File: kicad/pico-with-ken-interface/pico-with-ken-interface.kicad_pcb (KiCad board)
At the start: 4 copper layers, 81.3 x 81.3 mm, 10 parts, among them SW2 TSC015A03526A, U1 Pico, U3 XDZ254-2-15-W-2.5-G1, U5 PM254-2-15-W-8.5

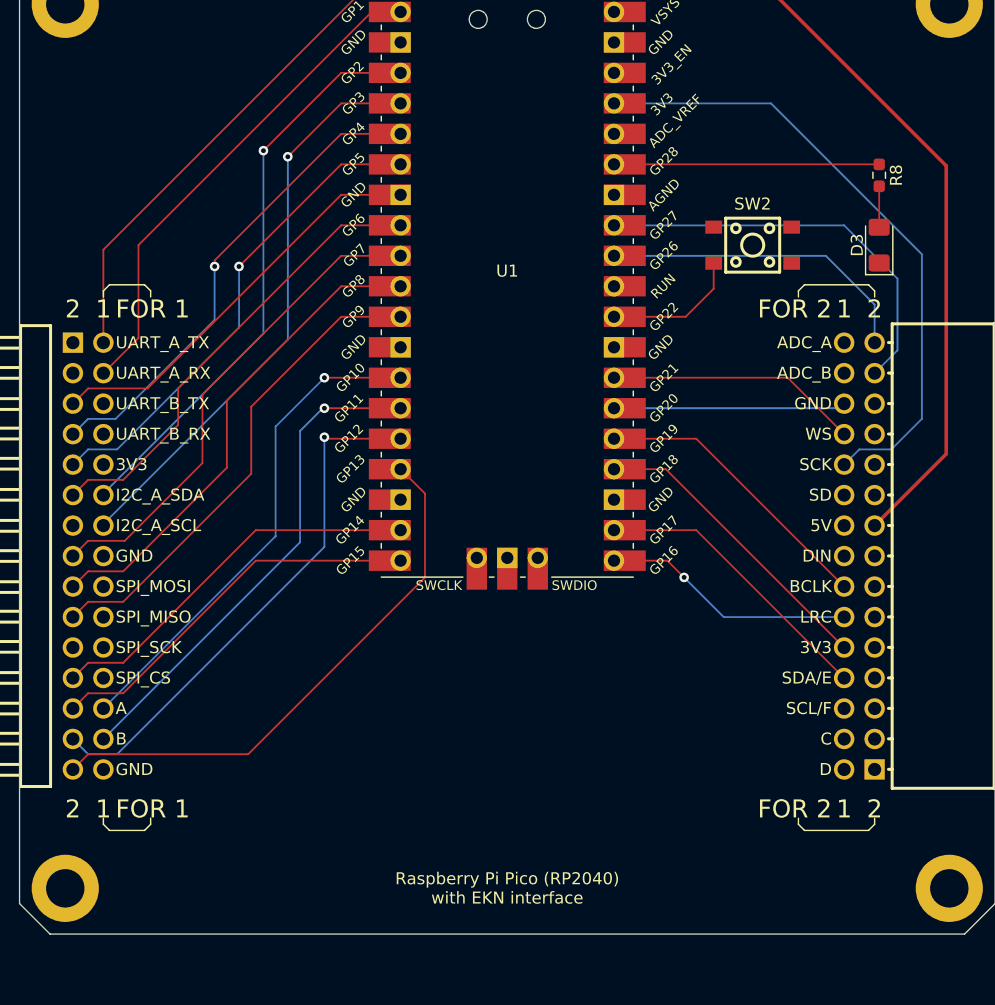
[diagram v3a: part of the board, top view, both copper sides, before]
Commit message: finalize pin assignment for pico board
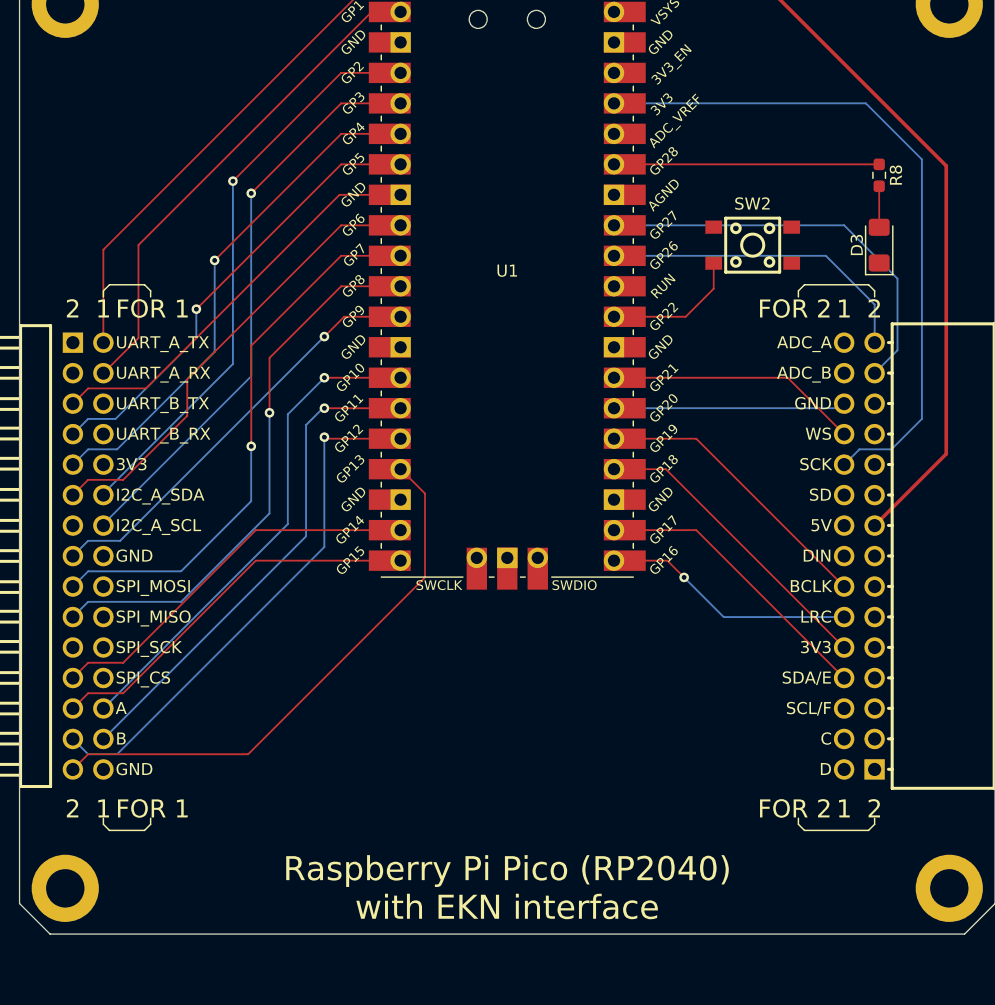
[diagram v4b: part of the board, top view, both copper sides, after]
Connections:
- U3 pad 15: /GPIO7 -> /GPIO9
- U3 pad 17: /GPIO8 -> /GPIO7
- U3 pad 19: /GPIO9 -> /GPIO8
- U3 pad 7: /GPIO4 -> /GPIO5
- U3 pad 9: /GPIO5 -> /GPIO4
- U5 pad 11: /GPIO9 -> /GPIO8
- U5 pad 13: /GPIO8 -> /GPIO7
- U5 pad 15: /GPIO7 -> /GPIO9
- U5 pad 21: /GPIO5 -> /GPIO4
- U5 pad 23: /GPIO4 -> /GPIO5
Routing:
- net +3V3: track 167.8 -> 172.5 mm
- net /GPIO8: track 117.6 -> 122.2 mm, vias 0 -> 1
- net /GPIO7: track 118.5 -> 123.0 mm, vias 0 -> 1
- net /GPIO9: track 116.8 -> 113.1 mm, vias 0 -> 1
- net /GPIO5: track 120.7 -> 118.9 mm
- net /GPIO4: track 121.5 -> 123.2 mm
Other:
- board text added: "version:1.0 date: 20260204"
- board text removed: "version:1.0 date: 20260202"

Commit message: trace adjust
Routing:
- net +5V: track 144.9 -> 145.9 mm

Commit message: ready to send pico board to manufacturing
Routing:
- net /GPIO8: track 122.2 -> 119.2 mm
- net /GPIO7: track 123.0 -> 120.0 mm
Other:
- board text added: "version:1.0 date: 20260211"
- board text removed: "version:1.0 date: 20260204"

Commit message: fix labels, update manufacture files
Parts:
- added kibuzzard-69ABCB94: G***, kibuzzard-69ABCB94, F.Cu at (119.5, 51.4)
- added kibuzzard-69ABCBB2: G***, kibuzzard-69ABCBB2, F.Cu at (130.0, 51.4)
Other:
- board text added: "Raspberry Pi Pico (RP2040) with EKN Interface"
- board text removed: "Raspberry Pi Pico (RP2040) with EKN interface"

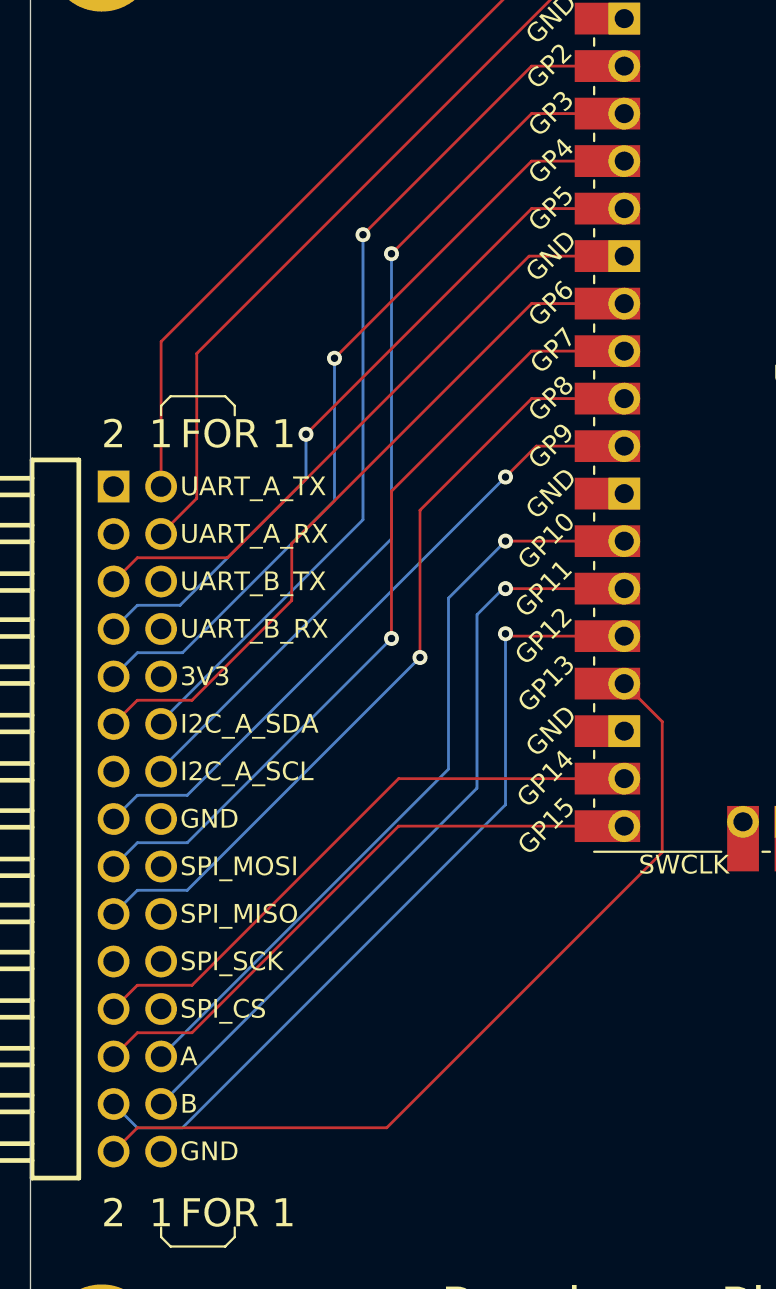
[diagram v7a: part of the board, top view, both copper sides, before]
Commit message: use 4,5 for default I2C pins
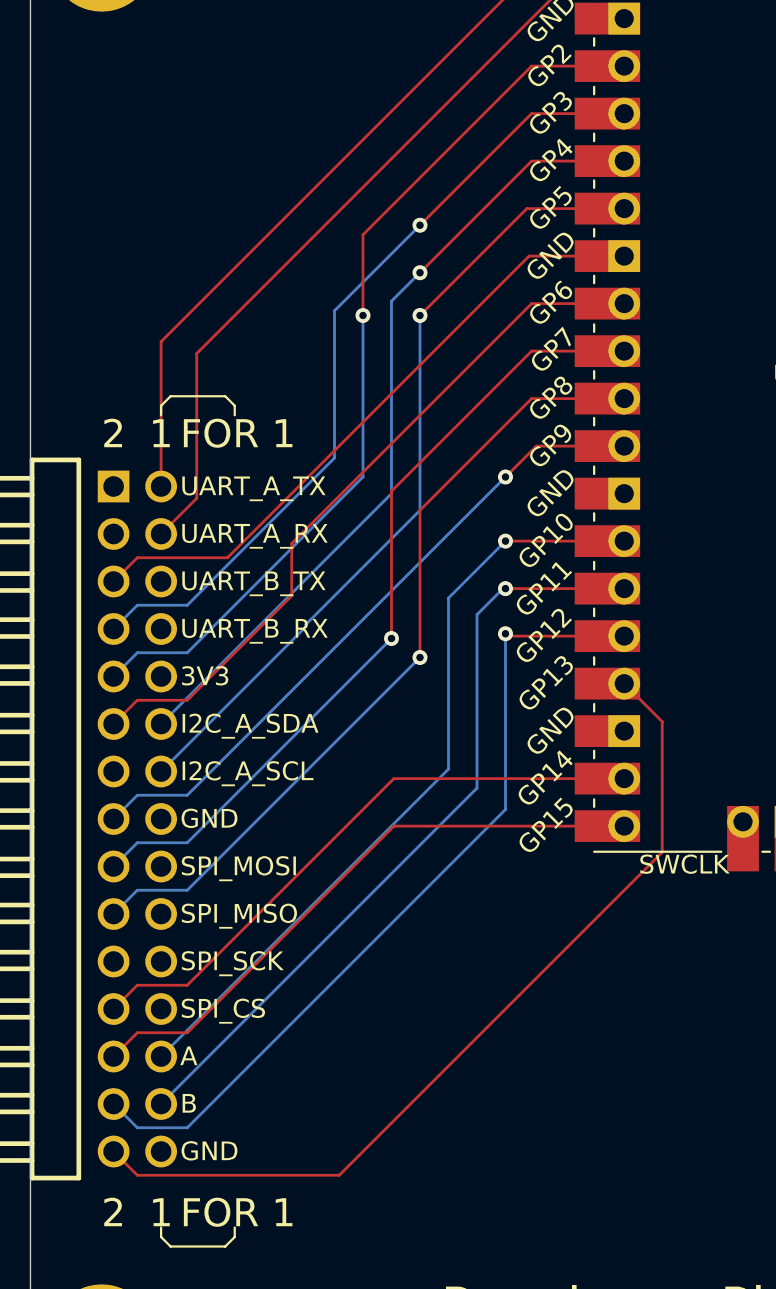
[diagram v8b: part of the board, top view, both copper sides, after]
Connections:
- U3 pad 12: /GPIO2 -> /GPIO4
- U3 pad 14: /GPIO3 -> /GPIO5
- U3 pad 7: /GPIO5 -> /GPIO3
- U3 pad 9: /GPIO4 -> /GPIO2
- U5 pad 18: /GPIO3 -> /GPIO5
- U5 pad 20: /GPIO2 -> /GPIO4
- U5 pad 21: /GPIO4 -> /GPIO2
- U5 pad 23: /GPIO5 -> /GPIO3
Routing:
- net /GPIO5: track 118.9 -> 121.2 mm
- net /GPIO3: track 126.0 -> 124.2 mm
- net /GPIO2: track 126.9 -> 128.5 mm
- net /GPIO4: track 123.2 -> 121.9 mm
- net /GPIO13: track 117.5 -> 118.5 mm
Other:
- board text added: "version:1.0 date: 20260312"
- board text removed: "version:1.0 date: 20260211"
